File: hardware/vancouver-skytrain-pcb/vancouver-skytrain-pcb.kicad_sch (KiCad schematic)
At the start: 156 parts, among them J2_POWER_IN1 Conn_01x02, J3_PROGRAMING_PIN1 Conn_01x06, Q1 PN2222A, Q2 PN2222A, U1 74AHC1G125, U2 74AHC1G125, U3 74AHC1G125, U4 74AHC1G125

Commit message: positioned all the LEDs, Cap, and 5v Rails
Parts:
- removed C71: 10uF,10V,X5R, vancouver-skytrain-pcb.pretty:C_0603_1608Metric, symbol jlcpcb-basic-capacitor-0603:10uF,10V,X5R
- removed C72, C73: 1uF,25V,X5R, vancouver-skytrain-pcb.pretty:C_0402_1005Metric, symbol jlcpcb-basic-capacitor-0402:1uF,25V,X5R
- removed LED64, LED65: WS2812B, LED_SMD:LED_WS2812B_PLCC4_5.0x5.0mm_P3.2mm, symbol calendar:XL-5050RGBC-WS2812B
- removed U2, U3, U4: 74AHC1G125, Package_TO_SOT_SMD:SOT-23-5, symbol 74xGxx:74AHC1G125
- added C100, C101, C102, C121, C122, C123, C124, C125, C126, C127, C128, C129, C130, C131, C132, C133, C134, C135, C136, C31, C32, C33, C34, C35, C36, C37, C38, C39, C40, C41, C42, C43, C44, C45, C46, C47, C48, C49, C50, C51, C52, C53, C54, C80, C81, C82, C83, C84, C85, C86, C87, C88, C89, C90, C91, C92, C93, C94, C95, C96, C97, C98, C99: 1uF,25V,X5R, vancouver-skytrain-pcb.pretty:C_0402_1005Metric, symbol jlcpcb-basic-capacitor-0402:1uF,25V,X5R
- added C120, C30, C79: 10uF,10V,X5R, vancouver-skytrain-pcb.pretty:C_0603_1608Metric, symbol jlcpcb-basic-capacitor-0603:10uF,10V,X5R
- added LED111, LED112, LED113, LED114, LED115, LED116, LED117, LED118, LED119, LED120, LED121, LED122, LED123, LED124, LED125, LED126, LED25, LED26, LED27, LED28, LED29, LED30, LED31, LED32, LED33, LED34, LED35, LED36, LED37, LED38, LED39, LED40, LED41, LED42, LED43, LED44, LED45, LED46, LED47, LED48, LED72, LED73, LED74, LED75, LED76, LED77, LED78, LED79, LED80, LED81, LED82, LED83, LED84, LED85, LED86, LED87, LED88, LED89, LED90, LED91, LED92, LED93, LED94: WS2812B, vancouver-skytrain-pcb.pretty:XL-1010RGBC-WS2812B, symbol vancouver-skytrain-pcb:XL-1010RGBC-WS2812B
- LED1, LED10, LED11, LED12, LED13, LED14, LED15, LED16, LED17, LED18, LED19, LED2, LED20, LED21, LED22, LED23, LED24, LED3, LED4, LED5, LED6, LED7, LED8, LED9: footprint LED_SMD:LED_WS2812B_PLCC4_5.0x5.0mm_P3.2mm -> vancouver-skytrain-pcb.pretty:XL-1010RGBC-WS2812B; symbol calendar:XL-5050RGBC-WS2812B -> vancouver-skytrain-pcb:XL-1010RGBC-WS2812B; LCSC C2843785 -> C5349953
- LED100: renamed from LED53; footprint LED_SMD:LED_WS2812B_PLCC4_5.0x5.0mm_P3.2mm -> vancouver-skytrain-pcb.pretty:XL-1010RGBC-WS2812B; symbol calendar:XL-5050RGBC-WS2812B -> vancouver-skytrain-pcb:XL-1010RGBC-WS2812B; LCSC C2843785 -> C5349953
- LED101: renamed from LED54; footprint LED_SMD:LED_WS2812B_PLCC4_5.0x5.0mm_P3.2mm -> vancouver-skytrain-pcb.pretty:XL-1010RGBC-WS2812B; symbol calendar:XL-5050RGBC-WS2812B -> vancouver-skytrain-pcb:XL-1010RGBC-WS2812B; LCSC C2843785 -> C5349953
- LED102: renamed from LED55; footprint LED_SMD:LED_WS2812B_PLCC4_5.0x5.0mm_P3.2mm -> vancouver-skytrain-pcb.pretty:XL-1010RGBC-WS2812B; symbol calendar:XL-5050RGBC-WS2812B -> vancouver-skytrain-pcb:XL-1010RGBC-WS2812B; LCSC C2843785 -> C5349953
- LED103: renamed from LED56; footprint LED_SMD:LED_WS2812B_PLCC4_5.0x5.0mm_P3.2mm -> vancouver-skytrain-pcb.pretty:XL-1010RGBC-WS2812B; symbol calendar:XL-5050RGBC-WS2812B -> vancouver-skytrain-pcb:XL-1010RGBC-WS2812B; LCSC C2843785 -> C5349953
- LED104: renamed from LED57; footprint LED_SMD:LED_WS2812B_PLCC4_5.0x5.0mm_P3.2mm -> vancouver-skytrain-pcb.pretty:XL-1010RGBC-WS2812B; symbol calendar:XL-5050RGBC-WS2812B -> vancouver-skytrain-pcb:XL-1010RGBC-WS2812B; LCSC C2843785 -> C5349953
- LED105: renamed from LED58; footprint LED_SMD:LED_WS2812B_PLCC4_5.0x5.0mm_P3.2mm -> vancouver-skytrain-pcb.pretty:XL-1010RGBC-WS2812B; symbol calendar:XL-5050RGBC-WS2812B -> vancouver-skytrain-pcb:XL-1010RGBC-WS2812B; LCSC C2843785 -> C5349953
- LED106: renamed from LED59; footprint LED_SMD:LED_WS2812B_PLCC4_5.0x5.0mm_P3.2mm -> vancouver-skytrain-pcb.pretty:XL-1010RGBC-WS2812B; symbol calendar:XL-5050RGBC-WS2812B -> vancouver-skytrain-pcb:XL-1010RGBC-WS2812B; LCSC C2843785 -> C5349953
- LED107: renamed from LED60; footprint LED_SMD:LED_WS2812B_PLCC4_5.0x5.0mm_P3.2mm -> vancouver-skytrain-pcb.pretty:XL-1010RGBC-WS2812B; symbol calendar:XL-5050RGBC-WS2812B -> vancouver-skytrain-pcb:XL-1010RGBC-WS2812B; LCSC C2843785 -> C5349953
- LED108: renamed from LED61; footprint LED_SMD:LED_WS2812B_PLCC4_5.0x5.0mm_P3.2mm -> vancouver-skytrain-pcb.pretty:XL-1010RGBC-WS2812B; symbol calendar:XL-5050RGBC-WS2812B -> vancouver-skytrain-pcb:XL-1010RGBC-WS2812B; LCSC C2843785 -> C5349953
- LED109: renamed from LED62; footprint LED_SMD:LED_WS2812B_PLCC4_5.0x5.0mm_P3.2mm -> vancouver-skytrain-pcb.pretty:XL-1010RGBC-WS2812B; symbol calendar:XL-5050RGBC-WS2812B -> vancouver-skytrain-pcb:XL-1010RGBC-WS2812B; LCSC C2843785 -> C5349953
- LED110: renamed from LED63; footprint LED_SMD:LED_WS2812B_PLCC4_5.0x5.0mm_P3.2mm -> vancouver-skytrain-pcb.pretty:XL-1010RGBC-WS2812B; symbol calendar:XL-5050RGBC-WS2812B -> vancouver-skytrain-pcb:XL-1010RGBC-WS2812B; LCSC C2843785 -> C5349953
- LED49: renamed from LED25; footprint LED_SMD:LED_WS2812B_PLCC4_5.0x5.0mm_P3.2mm -> vancouver-skytrain-pcb.pretty:XL-1010RGBC-WS2812B; symbol calendar:XL-5050RGBC-WS2812B -> vancouver-skytrain-pcb:XL-1010RGBC-WS2812B; LCSC C2843785 -> C5349953
- LED50: renamed from LED26; footprint LED_SMD:LED_WS2812B_PLCC4_5.0x5.0mm_P3.2mm -> vancouver-skytrain-pcb.pretty:XL-1010RGBC-WS2812B; symbol calendar:XL-5050RGBC-WS2812B -> vancouver-skytrain-pcb:XL-1010RGBC-WS2812B; LCSC C2843785 -> C5349953
- LED51: renamed from LED27; footprint LED_SMD:LED_WS2812B_PLCC4_5.0x5.0mm_P3.2mm -> vancouver-skytrain-pcb.pretty:XL-1010RGBC-WS2812B; symbol calendar:XL-5050RGBC-WS2812B -> vancouver-skytrain-pcb:XL-1010RGBC-WS2812B; LCSC C2843785 -> C5349953
- LED52: renamed from LED28; footprint LED_SMD:LED_WS2812B_PLCC4_5.0x5.0mm_P3.2mm -> vancouver-skytrain-pcb.pretty:XL-1010RGBC-WS2812B; symbol calendar:XL-5050RGBC-WS2812B -> vancouver-skytrain-pcb:XL-1010RGBC-WS2812B; LCSC C2843785 -> C5349953
- LED53: renamed from LED29; footprint LED_SMD:LED_WS2812B_PLCC4_5.0x5.0mm_P3.2mm -> vancouver-skytrain-pcb.pretty:XL-1010RGBC-WS2812B; symbol calendar:XL-5050RGBC-WS2812B -> vancouver-skytrain-pcb:XL-1010RGBC-WS2812B; LCSC C2843785 -> C5349953
- LED54: renamed from LED30; footprint LED_SMD:LED_WS2812B_PLCC4_5.0x5.0mm_P3.2mm -> vancouver-skytrain-pcb.pretty:XL-1010RGBC-WS2812B; symbol calendar:XL-5050RGBC-WS2812B -> vancouver-skytrain-pcb:XL-1010RGBC-WS2812B; LCSC C2843785 -> C5349953
- LED55: renamed from LED31; footprint LED_SMD:LED_WS2812B_PLCC4_5.0x5.0mm_P3.2mm -> vancouver-skytrain-pcb.pretty:XL-1010RGBC-WS2812B; symbol calendar:XL-5050RGBC-WS2812B -> vancouver-skytrain-pcb:XL-1010RGBC-WS2812B; LCSC C2843785 -> C5349953
- LED56: renamed from LED32; footprint LED_SMD:LED_WS2812B_PLCC4_5.0x5.0mm_P3.2mm -> vancouver-skytrain-pcb.pretty:XL-1010RGBC-WS2812B; symbol calendar:XL-5050RGBC-WS2812B -> vancouver-skytrain-pcb:XL-1010RGBC-WS2812B; LCSC C2843785 -> C5349953
- LED57: renamed from LED33; footprint LED_SMD:LED_WS2812B_PLCC4_5.0x5.0mm_P3.2mm -> vancouver-skytrain-pcb.pretty:XL-1010RGBC-WS2812B; symbol calendar:XL-5050RGBC-WS2812B -> vancouver-skytrain-pcb:XL-1010RGBC-WS2812B; LCSC C2843785 -> C5349953
- LED58: renamed from LED34; footprint LED_SMD:LED_WS2812B_PLCC4_5.0x5.0mm_P3.2mm -> vancouver-skytrain-pcb.pretty:XL-1010RGBC-WS2812B; symbol calendar:XL-5050RGBC-WS2812B -> vancouver-skytrain-pcb:XL-1010RGBC-WS2812B; LCSC C2843785 -> C5349953
- LED59: renamed from LED35; footprint LED_SMD:LED_WS2812B_PLCC4_5.0x5.0mm_P3.2mm -> vancouver-skytrain-pcb.pretty:XL-1010RGBC-WS2812B; symbol calendar:XL-5050RGBC-WS2812B -> vancouver-skytrain-pcb:XL-1010RGBC-WS2812B; LCSC C2843785 -> C5349953
- LED60: renamed from LED36; footprint LED_SMD:LED_WS2812B_PLCC4_5.0x5.0mm_P3.2mm -> vancouver-skytrain-pcb.pretty:XL-1010RGBC-WS2812B; symbol calendar:XL-5050RGBC-WS2812B -> vancouver-skytrain-pcb:XL-1010RGBC-WS2812B; LCSC C2843785 -> C5349953
- LED61: renamed from LED37; footprint LED_SMD:LED_WS2812B_PLCC4_5.0x5.0mm_P3.2mm -> vancouver-skytrain-pcb.pretty:XL-1010RGBC-WS2812B; symbol calendar:XL-5050RGBC-WS2812B -> vancouver-skytrain-pcb:XL-1010RGBC-WS2812B; LCSC C2843785 -> C5349953
- LED62: renamed from LED38; footprint LED_SMD:LED_WS2812B_PLCC4_5.0x5.0mm_P3.2mm -> vancouver-skytrain-pcb.pretty:XL-1010RGBC-WS2812B; symbol calendar:XL-5050RGBC-WS2812B -> vancouver-skytrain-pcb:XL-1010RGBC-WS2812B; LCSC C2843785 -> C5349953
- LED63: renamed from LED39; footprint LED_SMD:LED_WS2812B_PLCC4_5.0x5.0mm_P3.2mm -> vancouver-skytrain-pcb.pretty:XL-1010RGBC-WS2812B; symbol calendar:XL-5050RGBC-WS2812B -> vancouver-skytrain-pcb:XL-1010RGBC-WS2812B; LCSC C2843785 -> C5349953
- LED64: renamed from LED40; footprint LED_SMD:LED_WS2812B_PLCC4_5.0x5.0mm_P3.2mm -> vancouver-skytrain-pcb.pretty:XL-1010RGBC-WS2812B; symbol calendar:XL-5050RGBC-WS2812B -> vancouver-skytrain-pcb:XL-1010RGBC-WS2812B; LCSC C2843785 -> C5349953
- LED65: renamed from LED41; footprint LED_SMD:LED_WS2812B_PLCC4_5.0x5.0mm_P3.2mm -> vancouver-skytrain-pcb.pretty:XL-1010RGBC-WS2812B; symbol calendar:XL-5050RGBC-WS2812B -> vancouver-skytrain-pcb:XL-1010RGBC-WS2812B; LCSC C2843785 -> C5349953
- LED66: renamed from LED42; footprint LED_SMD:LED_WS2812B_PLCC4_5.0x5.0mm_P3.2mm -> vancouver-skytrain-pcb.pretty:XL-1010RGBC-WS2812B; symbol calendar:XL-5050RGBC-WS2812B -> vancouver-skytrain-pcb:XL-1010RGBC-WS2812B; LCSC C2843785 -> C5349953
- LED67: renamed from LED43; footprint LED_SMD:LED_WS2812B_PLCC4_5.0x5.0mm_P3.2mm -> vancouver-skytrain-pcb.pretty:XL-1010RGBC-WS2812B; symbol calendar:XL-5050RGBC-WS2812B -> vancouver-skytrain-pcb:XL-1010RGBC-WS2812B; LCSC C2843785 -> C5349953
- LED68: renamed from LED44; footprint LED_SMD:LED_WS2812B_PLCC4_5.0x5.0mm_P3.2mm -> vancouver-skytrain-pcb.pretty:XL-1010RGBC-WS2812B; symbol calendar:XL-5050RGBC-WS2812B -> vancouver-skytrain-pcb:XL-1010RGBC-WS2812B; LCSC C2843785 -> C5349953
- LED69: renamed from LED45; footprint LED_SMD:LED_WS2812B_PLCC4_5.0x5.0mm_P3.2mm -> vancouver-skytrain-pcb.pretty:XL-1010RGBC-WS2812B; symbol calendar:XL-5050RGBC-WS2812B -> vancouver-skytrain-pcb:XL-1010RGBC-WS2812B; LCSC C2843785 -> C5349953
- LED70: renamed from LED46; footprint LED_SMD:LED_WS2812B_PLCC4_5.0x5.0mm_P3.2mm -> vancouver-skytrain-pcb.pretty:XL-1010RGBC-WS2812B; symbol calendar:XL-5050RGBC-WS2812B -> vancouver-skytrain-pcb:XL-1010RGBC-WS2812B; LCSC C2843785 -> C5349953
- LED71: renamed from LED47; footprint LED_SMD:LED_WS2812B_PLCC4_5.0x5.0mm_P3.2mm -> vancouver-skytrain-pcb.pretty:XL-1010RGBC-WS2812B; symbol calendar:XL-5050RGBC-WS2812B -> vancouver-skytrain-pcb:XL-1010RGBC-WS2812B; LCSC C2843785 -> C5349953
- LED95: renamed from LED48; footprint LED_SMD:LED_WS2812B_PLCC4_5.0x5.0mm_P3.2mm -> vancouver-skytrain-pcb.pretty:XL-1010RGBC-WS2812B; symbol calendar:XL-5050RGBC-WS2812B -> vancouver-skytrain-pcb:XL-1010RGBC-WS2812B; LCSC C2843785 -> C5349953
- LED96: renamed from LED49; footprint LED_SMD:LED_WS2812B_PLCC4_5.0x5.0mm_P3.2mm -> vancouver-skytrain-pcb.pretty:XL-1010RGBC-WS2812B; symbol calendar:XL-5050RGBC-WS2812B -> vancouver-skytrain-pcb:XL-1010RGBC-WS2812B; LCSC C2843785 -> C5349953
- LED97: renamed from LED50; footprint LED_SMD:LED_WS2812B_PLCC4_5.0x5.0mm_P3.2mm -> vancouver-skytrain-pcb.pretty:XL-1010RGBC-WS2812B; symbol calendar:XL-5050RGBC-WS2812B -> vancouver-skytrain-pcb:XL-1010RGBC-WS2812B; LCSC C2843785 -> C5349953
- LED98: renamed from LED51; footprint LED_SMD:LED_WS2812B_PLCC4_5.0x5.0mm_P3.2mm -> vancouver-skytrain-pcb.pretty:XL-1010RGBC-WS2812B; symbol calendar:XL-5050RGBC-WS2812B -> vancouver-skytrain-pcb:XL-1010RGBC-WS2812B; LCSC C2843785 -> C5349953
- LED99: renamed from LED52; footprint LED_SMD:LED_WS2812B_PLCC4_5.0x5.0mm_P3.2mm -> vancouver-skytrain-pcb.pretty:XL-1010RGBC-WS2812B; symbol calendar:XL-5050RGBC-WS2812B -> vancouver-skytrain-pcb:XL-1010RGBC-WS2812B; LCSC C2843785 -> C5349953
- renumbered C54 to C103, C55 to C104, C56 to C105, C57 to C106, C58 to C107, C59 to C108, C60 to C109, C61 to C110, C62 to C111, C63 to C112, C64 to C113, C65 to C114, C66 to C115, C67 to C116, C68 to C117, C69 to C118, C70 to C119, C30 to C55, C31 to C56, C32 to C57, C33 to C58, C34 to C59, C35 to C60, C36 to C61, C37 to C62, C38 to C63, C39 to C64, C40 to C65, C41 to C66, C42 to C67, C43 to C68, C44 to C69, C45 to C70, C46 to C71, C47 to C72, C48 to C73, C49 to C74, C50 to C75, C51 to C76, C52 to C77, C53 to C78
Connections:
- net +5V: now also LED1.2 (VDD), LED10.2 (VDD), LED100.2 (VDD), LED101.2 (VDD), LED102.2 (VDD), LED103.2 (VDD), LED104.2 (VDD), LED105.2 (VDD), LED106.2 (VDD), LED107.2 (VDD), LED108.2 (VDD), LED109.2 (VDD), LED11.2 (VDD), LED110.2 (VDD), LED12.2 (VDD), LED13.2 (VDD), LED14.2 (VDD), LED15.2 (VDD), LED16.2 (VDD), LED17.2 (VDD), LED18.2 (VDD), LED19.2 (VDD), LED2.2 (VDD), LED20.2 (VDD), LED21.2 (VDD), LED22.2 (VDD), LED23.2 (VDD), LED24.2 (VDD), LED3.2 (VDD), LED4.2 (VDD), LED49.2 (VDD), LED5.2 (VDD), LED50.2 (VDD), LED51.2 (VDD), LED52.2 (VDD), LED53.2 (VDD), LED54.2 (VDD), LED55.2 (VDD), LED56.2 (VDD), LED57.2 (VDD)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; no longer LED1.1 (VDD), LED10.1 (VDD), LED100.1 (VDD), LED101.1 (VDD), LED102.1 (VDD), LED103.1 (VDD), LED104.1 (VDD), LED105.1 (VDD), LED106.1 (VDD), LED107.1 (VDD), LED108.1 (VDD), LED109.1 (VDD), LED11.1 (VDD), LED110.1 (VDD), LED12.1 (VDD), LED13.1 (VDD), LED14.1 (VDD), LED15.1 (VDD), LED16.1 (VDD), LED17.1 (VDD), LED18.1 (VDD), LED19.1 (VDD), LED2.1 (VDD), LED20.1 (VDD), LED21.1 (VDD), LED22.1 (VDD), LED23.1 (VDD), LED24.1 (VDD), LED3.1 (VDD), LED4.1 (VDD), LED49.1 (VDD), LED5.1 (VDD), LED50.1 (VDD), LED51.1 (VDD), LED52.1 (VDD), LED53.1 (VDD), LED54.1 (VDD), LED55.1 (VDD), LED56.1 (VDD), LED57.1 (VDD)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
- net GND: now also C100.2, C101.2, C102.2, C120.1, C121.2, C122.2, C123.2, C124.2, C125.2, C126.2, C127.2, C128.2, C129.2, C130.2, C131.2, C132.2, C133.2, C134.2, C135.2, C136.2, C30.1, C31.2, C32.2, C33.2, C34.2, C35.2, C36.2, C37.2, C38.2, C39.2, C40.2, C41.2, C42.2, C43.2, C44.2, C45.2, C46.2, C47.2, C48.2, C49.2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
- net SW_BRIGHTNESS: no longer U_CPU1.30 (IO18)
- net at LED70.4 (DIN): now also LED69.1 (DOUT); no longer LED69.2 (DOU)
- net at LED69.4 (DIN): now also LED68.1 (DOUT); no longer LED68.2 (DOU)
- net at LED24.4 (DIN): now also LED23.1 (DOUT); no longer LED23.2 (DOU)
- net at LED23.4 (DIN): now also LED22.1 (DOUT); no longer LED22.2 (DOU)
- net at LED20.4 (DIN): now also LED19.1 (DOUT); no longer LED19.2 (DOU)
- net at LED19.4 (DIN): now also LED18.1 (DOUT); no longer LED18.2 (DOU)
- net LEDS_EXPO_LINE_EAST_TO_WEST: now reaches LED1.4 (DIN), U1.4
- net LEDS_CANADA_LINE_SOUTH_TO_NORTH: now reaches LED95.4 (DIN)
- net LEDS_CANADA_LINE_SOUTH_TO_NORTH: now also LED94.1 (DOUT)
- net at LED18.4 (DIN): now also LED17.1 (DOUT); no longer LED17.2 (DOU)
- net at LED110.4 (DIN): now also LED109.1 (DOUT); no longer LED109.2 (DOU)
- net at LED109.4 (DIN): now also LED108.1 (DOUT); no longer LED108.2 (DOU)
- net at LED54.4 (DIN): now also LED53.1 (DOUT); no longer LED53.2 (DOU)
- net at LED53.4 (DIN): now also LED52.1 (DOUT); no longer LED52.2 (DOU)
- net at LED17.4 (DIN): now also LED16.1 (DOUT); no longer LED16.2 (DOU)
- net at LED106.4 (DIN): now also LED105.1 (DOUT); no longer LED105.2 (DOU)
- net at LED105.4 (DIN): now also LED104.1 (DOUT); no longer LED104.2 (DOU)
- net at LED16.4 (DIN): now also LED15.1 (DOUT); no longer LED15.2 (DOU)
- net at LED15.4 (DIN): now also LED14.1 (DOUT); no longer LED14.2 (DOU)
- net at LED11.4 (DIN): now also LED10.1 (DOUT); no longer LED10.2 (DOU)
- net at LED10.4 (DIN): now also LED9.1 (DOUT); no longer LED9.2 (DOU)
- net at LED71.4 (DIN): now also LED70.1 (DOUT); no longer LED70.2 (DOU)
- net at LED9.4 (DIN): now also LED8.1 (DOUT); no longer LED8.2 (DOU)
- net at LED8.4 (DIN): now also LED7.1 (DOUT); no longer LED7.2 (DOU)
- net at LED63.4 (DIN): now also LED62.1 (DOUT); no longer LED62.2 (DOU)
- net at LED62.4 (DIN): now also LED61.1 (DOUT); no longer LED61.2 (DOU)
- net at LED108.4 (DIN): now also LED107.1 (DOUT); no longer LED107.2 (DOU)
- net at LED50.4 (DIN): now also LED49.1 (DOUT); no longer LED49.2 (DOU)
- net LEDS_MILLENNIUM_LINE_EAST_TO_WEST: now reaches LED49.4 (DIN)
- net LEDS_MILLENNIUM_LINE_EAST_TO_WEST: now also LED48.1 (DOUT)
- net at LED65.4 (DIN): now also LED64.1 (DOUT); no longer LED64.2 (DOU)
- net at LED64.4 (DIN): now also LED63.1 (DOUT); no longer LED63.2 (DOU)
- net at LED98.4 (DIN): now also LED97.1 (DOUT); no longer LED97.2 (DOU)
- net at LED97.4 (DIN): now also LED96.1 (DOUT); no longer LED96.2 (DOU)
- net at LED52.4 (DIN): now also LED51.1 (DOUT); no longer LED51.2 (DOU)
- net at LED14.4 (DIN): now also LED13.1 (DOUT); no longer LED13.2 (DOU)
- net at LED61.4 (DIN): now also LED60.1 (DOUT); no longer LED60.2 (DOU)
- net at LED96.4 (DIN): now also LED95.1 (DOUT); no longer LED95.2 (DOU)
- net at LED107.4 (DIN): now also LED106.1 (DOUT); no longer LED106.2 (DOU)
- net at LED51.4 (DIN): now also LED50.1 (DOUT); no longer LED50.2 (DOU)
- net at LED55.4 (DIN): now also LED54.1 (DOUT); no longer LED54.2 (DOU)
- net at LED5.4 (DIN): now also LED4.1 (DOUT); no longer LED4.2 (DOU)
- net at LED4.4 (DIN): now also LED3.1 (DOUT); no longer LED3.2 (DOU)
- net at LED104.4 (DIN): now also LED103.1 (DOUT); no longer LED103.2 (DOU)
- net at LED103.4 (DIN): now also LED102.1 (DOUT); no longer LED102.2 (DOU)
- net at LED13.4 (DIN): now also LED12.1 (DOUT); no longer LED12.2 (DOU)
- net at LED12.4 (DIN): now also LED11.1 (DOUT); no longer LED11.2 (DOU)
- net at LED57.4 (DIN): now also LED56.1 (DOUT); no longer LED56.2 (DOU)
- net at LED56.4 (DIN): now also LED55.1 (DOUT); no longer LED55.2 (DOU)
- net at LED67.4 (DIN): now also LED66.1 (DOUT); no longer LED66.2 (DOU)
- net at LED66.4 (DIN): now also LED65.1 (DOUT); no longer LED65.2 (DOU)
- net at LED99.4 (DIN): now also LED98.1 (DOUT); no longer LED98.2 (DOU)
- net at LED100.4 (DIN): now also LED99.1 (DOUT); no longer LED99.2 (DOU)
- net at LED7.4 (DIN): now also LED6.1 (DOUT); no longer LED6.2 (DOU)
- net at LED6.4 (DIN): now also LED5.1 (DOUT); no longer LED5.2 (DOU)
- net at LED22.4 (DIN): now also LED21.1 (DOUT); no longer LED21.2 (DOU)
- net at LED21.4 (DIN): now also LED20.1 (DOUT); no longer LED20.2 (DOU)
- net at LED68.4 (DIN): now also LED67.1 (DOUT); no longer LED67.2 (DOU)
- net at LED102.4 (DIN): now also LED101.1 (DOUT); no longer LED101.2 (DOU)
- net at LED2.4 (DIN): now also LED1.1 (DOUT); no longer LED1.2 (DOU)
- net at LED58.4 (DIN): now also LED57.1 (DOUT); no longer LED57.2 (DOU)
- net at LED59.4 (DIN): now also LED58.1 (DOUT); no longer LED58.2 (DOU)
- net at LED101.4 (DIN): now also LED100.1 (DOUT); no longer LED100.2 (DOU)
- net at LED60.4 (DIN): now also LED59.1 (DOUT); no longer LED59.2 (DOU)
- net at LED3.4 (DIN): now also LED2.1 (DOUT); no longer LED2.2 (DOU)
- net LEDS_CANADA_LINE: no longer names the net of U_CPU1.27 (IO16)
- net LEDS_EXPO_LINE renamed LED_IN
- net LEDS_MILLENNIUM_LINE: no longer names the net of U_CPU1.23 (IO15)
- net LEDS_SEA_BUS_LINE: no longer names the net of U_CPU1.28 (IO17)
- new net: LED80.1 (DOUT), LED81.4 (DIN)
- new net: LED79.1 (DOUT), LED80.4 (DIN)
- new net: LED27.1 (DOUT), LED28.4 (DIN)
- new net: LED26.1 (DOUT), LED27.4 (DIN)
- new net: LED77.1 (DOUT), LED78.4 (DIN)
- new net: LED76.1 (DOUT), LED77.4 (DIN)
- new net: LED90.1 (DOUT), LED91.4 (DIN)
- new net: LED89.1 (DOUT), LED90.4 (DIN)
- new net: LED42.1 (DOUT), LED43.4 (DIN)
- new net: LED41.1 (DOUT), LED42.4 (DIN)
- new net: LED73.1 (DOUT), LED74.4 (DIN)
- new net: LED72.1 (DOUT), LED73.4 (DIN)
- new net: LED124.1 (DOUT), LED125.4 (DIN)
- new net: LED123.1 (DOUT), LED124.4 (DIN)
- new net: LED29.1 (DOUT), LED30.4 (DIN)
- new net: LED28.1 (DOUT), LED29.4 (DIN)
- new net: LED112.1 (DOUT), LED113.4 (DIN)
- new net: LED111.1 (DOUT), LED112.4 (DIN)
- new net: LED34.1 (DOUT), LED35.4 (DIN)
- new net: LED33.1 (DOUT), LED34.4 (DIN)
- new net: LED40.1 (DOUT), LED41.4 (DIN)
- new net: LED39.1 (DOUT), LED40.4 (DIN)
- new net: LED25.1 (DOUT), LED26.4 (DIN)
- new net: LED120.1 (DOUT), LED121.4 (DIN)
- new net: LED119.1 (DOUT), LED120.4 (DIN)
- new net: LED37.1 (DOUT), LED38.4 (DIN)
- new net: LED36.1 (DOUT), LED37.4 (DIN)
- new net: LED35.1 (DOUT), LED36.4 (DIN)
- new net: LED83.1 (DOUT), LED84.4 (DIN)
- new net: LED82.1 (DOUT), LED83.4 (DIN)
- new net: LED91.1 (DOUT), LED92.4 (DIN)
- new net: LED38.1 (DOUT), LED39.4 (DIN)
- new net: LED87.1 (DOUT), LED88.4 (DIN)
- new net: LED86.1 (DOUT), LED87.4 (DIN)
- new net: LED45.1 (DOUT), LED46.4 (DIN)
- new net: LED44.1 (DOUT), LED45.4 (DIN)
- new net: LED125.1 (DOUT), LED126.4 (DIN)
- new net: LED47.1 (DOUT), LED48.4 (DIN)
- new net: LED114.1 (DOUT), LED115.4 (DIN)
- new net: LED113.1 (DOUT), LED114.4 (DIN)
- new net: LED93.1 (DOUT), LED94.4 (DIN)
- new net: LED92.1 (DOUT), LED93.4 (DIN)
- new net: LED74.1 (DOUT), LED75.4 (DIN)
- new net: LED117.1 (DOUT), LED118.4 (DIN)
- new net: LED116.1 (DOUT), LED117.4 (DIN)
- new net: LED46.1 (DOUT), LED47.4 (DIN)
- new net: LED75.1 (DOUT), LED76.4 (DIN)
- new net: LED121.1 (DOUT), LED122.4 (DIN)
- new net: LED81.1 (DOUT), LED82.4 (DIN)
- new net: LED43.1 (DOUT), LED44.4 (DIN)
- new net: LED118.1 (DOUT), LED119.4 (DIN)
- new net: LED85.1 (DOUT), LED86.4 (DIN)
- new net: LED115.1 (DOUT), LED116.4 (DIN)
- new net: LED32.1 (DOUT), LED33.4 (DIN)
- new net: LED88.1 (DOUT), LED89.4 (DIN)
- new net: LED31.1 (DOUT), LED32.4 (DIN)
- new net: LED30.1 (DOUT), LED31.4 (DIN)
- new net: LED84.1 (DOUT), LED85.4 (DIN)
- new net: LED122.1 (DOUT), LED123.4 (DIN)
- new net: LED78.1 (DOUT), LED79.4 (DIN)
- new net LEDS_CANADA_LINE_NORTH_TO_SOUTH: LED110.1 (DOUT), LED111.4 (DIN)
- new net LEDS_EXPO_LINE_WEST_TO_EAST: LED24.1 (DOUT), LED25.4 (DIN)
- new net LEDS_MILLENNIUM_LINE_WEST_TO_EAST: LED71.1 (DOUT), LED72.4 (DIN)
- new net LED_OUT: LED126.1 (DOUT)
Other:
- moved on the sheet: C103, C104, C105, C106, C107, C108, C109, C110, C111, C112, C113, C114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

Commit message: Resolved a bunch of DRC errors
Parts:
- removed C103, C120, C30, C5, C55, C79: 10uF,10V,X5R, vancouver-skytrain-pcb.pretty:C_0603_1608Metric, symbol jlcpcb-basic-capacitor-0603:10uF,10V,X5R
- removed SW_BRIGHTNESS1: Switch_SW_Push, Button_Switch_SMD:SW_Push_1P1T_NO_6x6mm_H9.5mm, symbol tom-mechanical:SW_SPST
- added C131: 1uF,25V,X5R, vancouver-skytrain-pcb.pretty:C_0402_1005Metric, symbol jlcpcb-basic-capacitor-0402:1uF,25V,X5R
- added H1, H2, H3, H4: MountingHole, MountingHole:MountingHole_3.2mm_M3, symbol Mechanical:MountingHole
- added J1: Conn_01x04, Connector_PinHeader_2.54mm:PinHeader_1x04_P2.54mm_Vertical, symbol Connector_Generic:Conn_01x04
- added LED127: WS2812B, vancouver-skytrain-pcb.pretty:XL-1010RGBC-WS2812B, symbol vancouver-skytrain-pcb:XL-1010RGBC-WS2812B
- added R2: 0, Resistor_SMD:R_0402_1005Metric, symbol jlcpcb-basic-resistor-0402:0
- renumbered C11 to C10, C105 to C100, C106 to C101, C107 to C102, C108 to C103, C109 to C104, C110 to C105, C111 to C106, C112 to C107, C113 to C108, C114 to C109, C12 to C11, C115 to C110, C116 to C111, C117 to C112, C118 to C113, C119 to C114, C121 to C115, C122 to C116, C123 to C117, C124 to C118, C125 to C119, C13 to C12, C126 to C120, C127 to C121, C128 to C122, C129 to C123, C130 to C124, C131 to C125, C132 to C126, C133 to C127, C134 to C128, C135 to C129, C14 to C13, C136 to C130, C15 to C14, C16 to C15, C17 to C16, C18 to C17, C19 to C18, C20 to C19, C21 to C20, C22 to C21, C23 to C22, C24 to C23, C25 to C24, C26 to C25, C27 to C26, C28 to C27, C29 to C28, C31 to C29, C32 to C30, C33 to C31, C34 to C32, C35 to C33, C36 to C34, C37 to C35, C38 to C36, C39 to C37, C40 to C38, C41 to C39, C42 to C40, C43 to C41, C44 to C42, C45 to C43, C46 to C44, C47 to C45, C48 to C46, C49 to C47, C50 to C48, C51 to C49, C6 to C5, C52 to C50, C53 to C51, C54 to C52, C56 to C53, C57 to C54, C58 to C55, C59 to C56, C60 to C57, C61 to C58, C62 to C59, C7 to C6, C63 to C60, C64 to C61, C65 to C62, C66 to C63, C67 to C64, C68 to C65, C69 to C66, C70 to C67, C71 to C68, C72 to C69, C8 to C7, C73 to C70, C74 to C71, C75 to C72, C76 to C73, C77 to C74, C78 to C75, C80 to C76, C81 to C77, C82 to C78, C83 to C79, C9 to C8, C84 to C80, C85 to C81, C86 to C82, C87 to C83, C88 to C84, C89 to C85, C90 to C86, C91 to C87, C92 to C88, C93 to C89, C10 to C9, C94 to C90, C95 to C91, C96 to C92, C97 to C93, C98 to C94, C99 to C95, C100 to C96, C101 to C97, C102 to C98, C104 to C99, R2 to R3, R3 to R4, R4 to R5
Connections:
- net +5V: now also C131.1, J1.1 (Pin_1), LED127.2 (VDD)
- net GND: now also C131.2, J1.3 (Pin_3), LED127.3 (VSS)
- net LED_IN: now also J1.2 (Pin_2), R2.2; no longer U_CPU1.13 (IO14)
- net LED_OUT: now also J1.4 (Pin_4), LED127.1 (DOUT); no longer LED126.1 (DOUT)
- new net: R2.1, U_CPU1.13 (IO14)
- new net LEDS_SEA_BUS: LED126.1 (DOUT), LED127.4 (DIN)
- no-connect marks 3 -> 22

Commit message: Clean up before sending to fab
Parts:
- U_POWER1: value LT1117-3.3 -> UR133AG-33-AB3-C-R__3.3v; footprint Package_TO_SOT_SMD:TO-263-3_TabPin2 -> Package_TO_SOT_SMD:SOT-89-3; LCSC C498315 -> C73288
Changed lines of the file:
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@@
   )
   (symbol (lib_id "Regulator_Linear:LT1117-3.3") (at 130.175 36.195 0) (unit 1)
-    (in_bom yes) (on_board yes) (dnp no) (fields_autoplaced)
+    (in_bom yes) (on_board yes) (dnp no)
     (property "Reference" "U_POWER1" (at 130.175 28.575 0)
       (effects (font (size 1.27 1.27)))
     )
-    (property "Value" "LT1117-3.3" (at 130.175 31.115 0)
+    (property "Value" "UR133AG-33-AB3-C-R__3.3v" (at 130.81 25.4 0)
       (effects (font (size 1.27 1.27)))
     )
-    (property "Footprint" "Package_TO_SOT_SMD:TO-263-3_TabPin2" (at 130.175 36.195 0)
+    (property "Footprint" "Package_TO_SOT_SMD:SOT-89-3" (at 130.175 36.195 0)
       (effects (font (size 1.27 1.27)) hide)
     )
-    (property "Datasheet" "https://www.analog.com/media/en/technical-documentation/data-sheets/1117fd.pdf" (at 130.175 36.195 0)
+    (property "Datasheet" "https://datasheet.lcsc.com/lcsc/2304140030_UTC-Unisonic-Tech-UR133AG-33-AB3-C-R_C73288.pdf" (at 130.175 36.195 0)
       (effects (font (size 1.27 1.27)) hide)
     )
-    (property "LCSC" "C498315" (at 130.175 36.195 0)
+    (property "LCSC" "C73288" (at 130.175 36.195 0)
       (effects (font (size 1.27 1.27)) hide)
     )

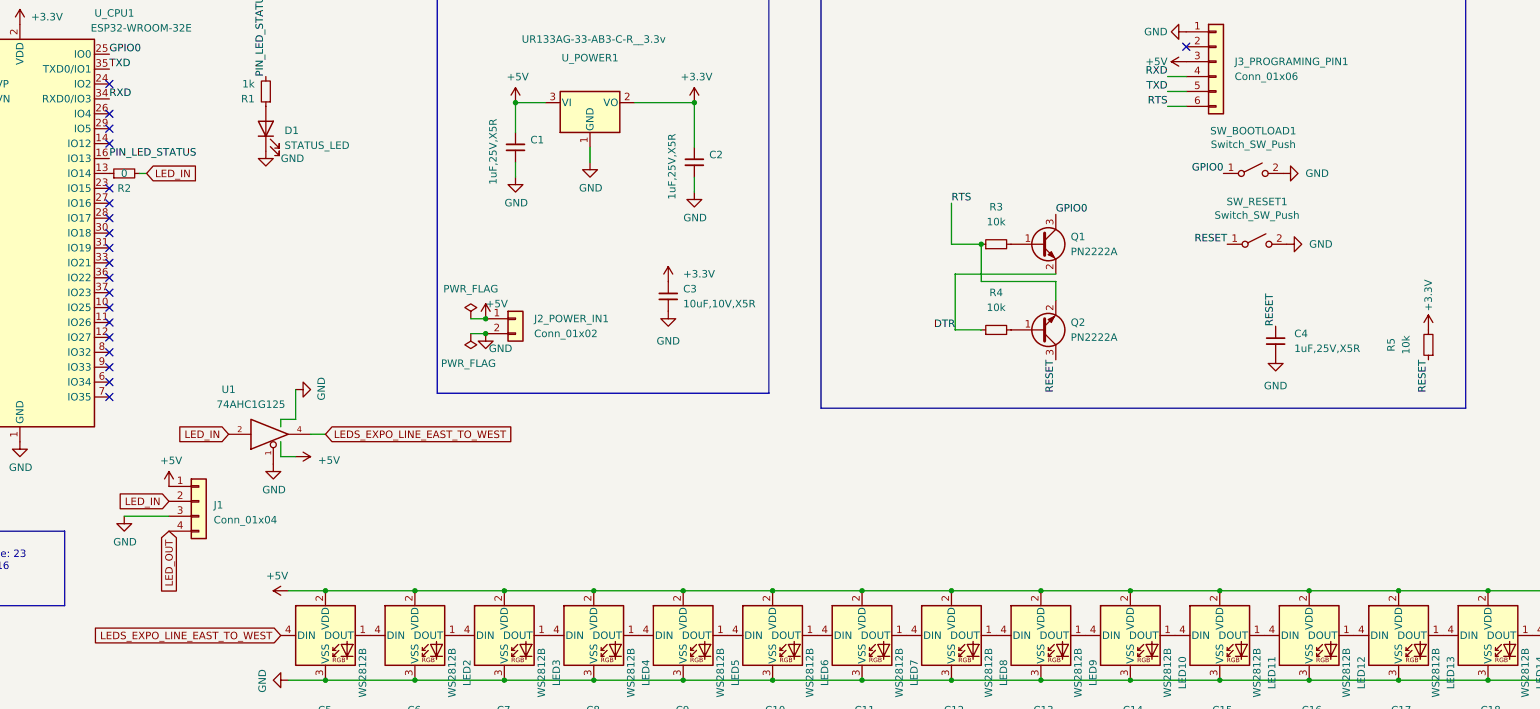
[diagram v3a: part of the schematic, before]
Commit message: Updated headers and update to kicad v8
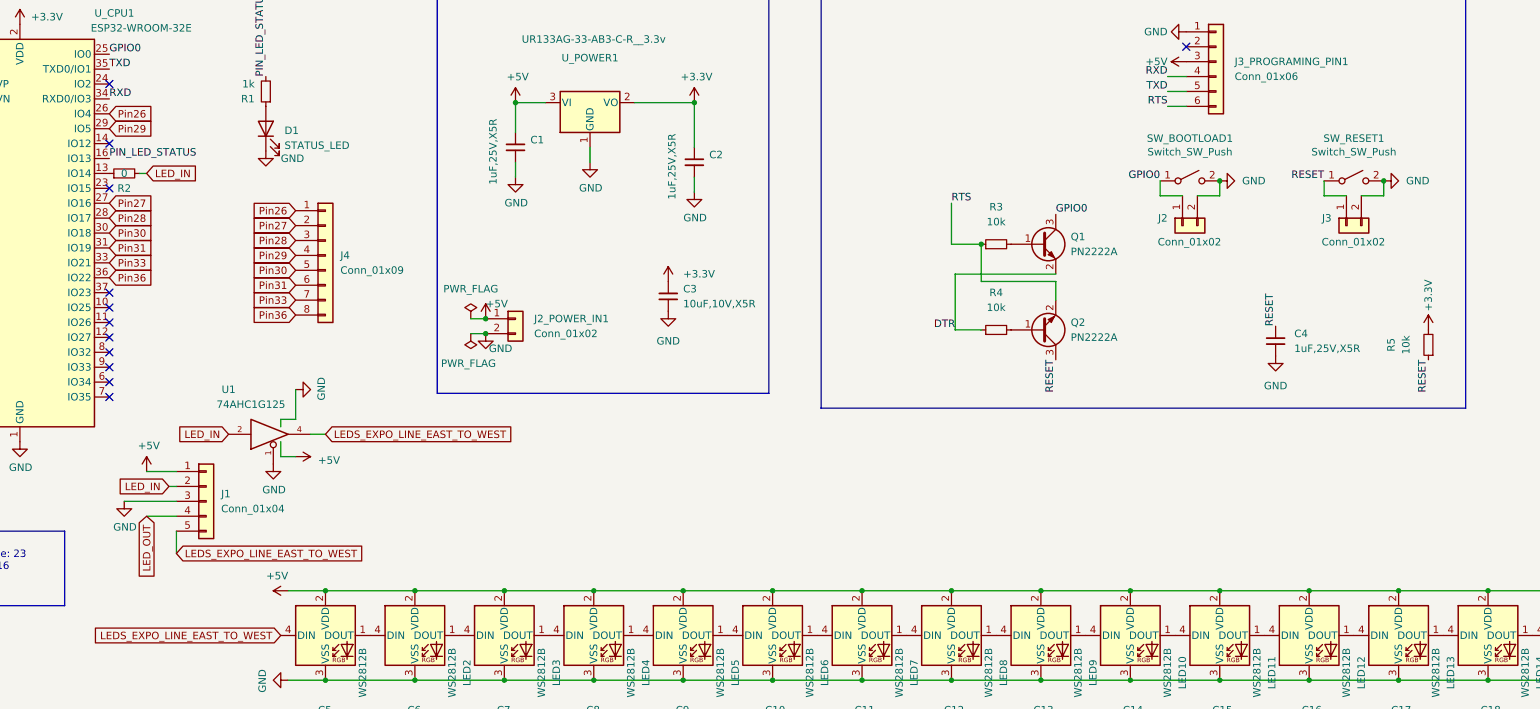
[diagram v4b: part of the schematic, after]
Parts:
- added J2, J3: Conn_01x02, Connector_PinHeader_2.54mm:PinHeader_1x02_P2.54mm_Vertical, symbol Connector_Generic:Conn_01x02
- added J4: Conn_01x09, Connector_PinHeader_2.54mm:PinHeader_1x08_P2.54mm_Vertical, symbol Connector_Generic:Conn_01x08
- J1: footprint Connector_PinHeader_2.54mm:PinHeader_1x04_P2.54mm_Vertical -> Connector_PinHeader_2.54mm:PinHeader_1x05_P2.54mm_Vertical; symbol Connector_Generic:Conn_01x04 -> Connector_Generic:Conn_01x05
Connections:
- net GND: now also J2.2 (Pin_2), J3.2 (Pin_2)
- net GPIO0: now also J2.1 (Pin_1)
- net LEDS_EXPO_LINE_EAST_TO_WEST: now also J1.5 (Pin_5)
- net RESET: now also J3.1 (Pin_1)
- net Pin26: now reaches U_CPU1.26 (IO4)
- net Pin26: now also J4.1 (Pin_1)
- net Pin27: now reaches U_CPU1.27 (IO16)
- net Pin27: now also J4.2 (Pin_2)
- net Pin28: now reaches U_CPU1.28 (IO17)
- net Pin28: now also J4.3 (Pin_3)
- net Pin29: now reaches U_CPU1.29 (IO5)
- net Pin29: now also J4.4 (Pin_4)
- net Pin30: now reaches U_CPU1.30 (IO18)
- net Pin30: now also J4.5 (Pin_5)
- net Pin31: now reaches U_CPU1.31 (IO19)
- net Pin31: now also J4.6 (Pin_6)
- net Pin33: now reaches U_CPU1.33 (IO21)
- net Pin33: now also J4.7 (Pin_7)
- net Pin36: now reaches U_CPU1.36 (IO22)
- net Pin36: now also J4.8 (Pin_8)
- no-connect marks 22 -> 14
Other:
- moved on the sheet: SW_BOOTLOAD1, SW_RESET1

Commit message: Added test points for all leds that look like bugs
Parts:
- added TP1, TP10, TP100, TP101, TP102, TP103, TP104, TP105, TP106, TP107, TP108, TP109, TP11, TP110, TP111, TP112, TP113, TP114, TP115, TP116, TP117, TP118, TP119, TP12, TP120, TP121, TP122, TP123, TP124, TP125, TP126, TP13, TP14, TP15, TP16, TP17, TP18, TP19, TP2, TP20, TP21, TP22, TP23, TP24, TP25, TP26, TP27, TP28, TP29, TP3, TP30, TP31, TP32, TP33, TP34, TP35, TP36, TP37, TP38, TP39, TP4, TP40, TP41, TP42, TP43, TP44, TP45, TP46, TP47, TP48, TP49, TP5, TP50, TP51, TP52, TP53, TP54, TP55, TP56, TP57, TP58, TP59, TP6, TP60, TP61, TP62, TP63, TP64, TP65, TP66, TP67, TP68, TP69, TP7, TP70, TP71, TP72, TP73, TP74, TP75, TP76, TP77, TP78, TP79, TP8, TP80, TP81, TP82, TP83, TP84, TP85, TP86, TP87, TP88, TP89, TP9, TP90, TP91, TP92, TP93, TP94, TP95, TP96, TP97, TP98, TP99: TestPoint, SWS-Library:SWS-Testpoint-Bug-1mm, symbol Connector:TestPoint
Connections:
- net LEDS_CANADA_LINE_NORTH_TO_SOUTH: now also TP110.1
- net LEDS_CANADA_LINE_SOUTH_TO_NORTH: now also TP94.1
- net LEDS_EXPO_LINE_WEST_TO_EAST: now also TP24.1
- net LEDS_MILLENNIUM_LINE_EAST_TO_WEST: now also TP48.1
- net LEDS_MILLENNIUM_LINE_WEST_TO_EAST: now also TP71.1
- net LEDS_SEA_BUS: now also TP126.1
- net at LED80.1 (DOUT), LED81.4 (DIN): now also TP80.1
- net at LED79.1 (DOUT), LED80.4 (DIN): now also TP79.1
- net at LED69.1 (DOUT), LED70.4 (DIN): now also TP69.1
- net at LED68.1 (DOUT), LED69.4 (DIN): now also TP68.1
- net at LED23.1 (DOUT), LED24.4 (DIN): now also TP23.1
- net at LED22.1 (DOUT), LED23.4 (DIN): now also TP22.1
- net at LED19.1 (DOUT), LED20.4 (DIN): now also TP19.1
- net at LED18.1 (DOUT), LED19.4 (DIN): now also TP18.1
- net at LED27.1 (DOUT), LED28.4 (DIN): now also TP27.1
- net at LED26.1 (DOUT), LED27.4 (DIN): now also TP26.1
- net at LED77.1 (DOUT), LED78.4 (DIN): now also TP77.1
- net at LED76.1 (DOUT), LED77.4 (DIN): now also TP76.1
- net at LED90.1 (DOUT), LED91.4 (DIN): now also TP90.1
- net at LED89.1 (DOUT), LED90.4 (DIN): now also TP89.1
- net at LED42.1 (DOUT), LED43.4 (DIN): now also TP42.1
- net at LED41.1 (DOUT), LED42.4 (DIN): now also TP41.1
- net at LED73.1 (DOUT), LED74.4 (DIN): now also TP73.1
- net at LED72.1 (DOUT), LED73.4 (DIN): now also TP72.1
- net at LED124.1 (DOUT), LED125.4 (DIN): now also TP124.1
- net at LED123.1 (DOUT), LED124.4 (DIN): now also TP123.1
- net at LED17.1 (DOUT), LED18.4 (DIN): now also TP17.1
- net at LED109.1 (DOUT), LED110.4 (DIN): now also TP109.1
- net at LED108.1 (DOUT), LED109.4 (DIN): now also TP108.1
- net at LED29.1 (DOUT), LED30.4 (DIN): now also TP29.1
- net at LED28.1 (DOUT), LED29.4 (DIN): now also TP28.1
- net at LED53.1 (DOUT), LED54.4 (DIN): now also TP53.1
- net at LED52.1 (DOUT), LED53.4 (DIN): now also TP52.1
- net at LED16.1 (DOUT), LED17.4 (DIN): now also TP16.1
- net at LED112.1 (DOUT), LED113.4 (DIN): now also TP112.1
- net at LED111.1 (DOUT), LED112.4 (DIN): now also TP111.1
- net at LED105.1 (DOUT), LED106.4 (DIN): now also TP105.1
- net at LED104.1 (DOUT), LED105.4 (DIN): now also TP104.1
- net at LED34.1 (DOUT), LED35.4 (DIN): now also TP34.1
- net at LED33.1 (DOUT), LED34.4 (DIN): now also TP33.1
- net at LED40.1 (DOUT), LED41.4 (DIN): now also TP40.1
- net at LED39.1 (DOUT), LED40.4 (DIN): now also TP39.1
- net at LED25.1 (DOUT), LED26.4 (DIN): now also TP25.1
- net at LED120.1 (DOUT), LED121.4 (DIN): now also TP120.1
- net at LED119.1 (DOUT), LED120.4 (DIN): now also TP119.1
- net at LED15.1 (DOUT), LED16.4 (DIN): now also TP15.1
- net at LED14.1 (DOUT), LED15.4 (DIN): now also TP14.1
- net at LED37.1 (DOUT), LED38.4 (DIN): now also TP37.1
- net at LED36.1 (DOUT), LED37.4 (DIN): now also TP36.1
- net at LED10.1 (DOUT), LED11.4 (DIN): now also TP10.1
- net at LED10.4 (DIN), LED9.1 (DOUT): now also TP9.1
- net at LED70.1 (DOUT), LED71.4 (DIN): now also TP70.1
- net at LED8.1 (DOUT), LED9.4 (DIN): now also TP8.1
- net at LED7.1 (DOUT), LED8.4 (DIN): now also TP7.1
- net at LED62.1 (DOUT), LED63.4 (DIN): now also TP62.1
- net at LED61.1 (DOUT), LED62.4 (DIN): now also TP61.1
- net at LED35.1 (DOUT), LED36.4 (DIN): now also TP35.1
- net at LED83.1 (DOUT), LED84.4 (DIN): now also TP83.1
- net at LED82.1 (DOUT), LED83.4 (DIN): now also TP82.1
- net at LED91.1 (DOUT), LED92.4 (DIN): now also TP91.1
- net at LED38.1 (DOUT), LED39.4 (DIN): now also TP38.1
- net at LED87.1 (DOUT), LED88.4 (DIN): now also TP87.1
- net at LED86.1 (DOUT), LED87.4 (DIN): now also TP86.1
- net at LED107.1 (DOUT), LED108.4 (DIN): now also TP107.1
- net at LED49.1 (DOUT), LED50.4 (DIN): now also TP49.1
- net at LED64.1 (DOUT), LED65.4 (DIN): now also TP64.1
- net at LED63.1 (DOUT), LED64.4 (DIN): now also TP63.1
- net at LED45.1 (DOUT), LED46.4 (DIN): now also TP45.1
- net at LED44.1 (DOUT), LED45.4 (DIN): now also TP44.1
- net at LED97.1 (DOUT), LED98.4 (DIN): now also TP97.1
- net at LED96.1 (DOUT), LED97.4 (DIN): now also TP96.1
- net at LED51.1 (DOUT), LED52.4 (DIN): now also TP51.1
- net at LED13.1 (DOUT), LED14.4 (DIN): now also TP13.1
- net at LED125.1 (DOUT), LED126.4 (DIN): now also TP125.1
- net at LED60.1 (DOUT), LED61.4 (DIN): now also TP60.1
- net at LED47.1 (DOUT), LED48.4 (DIN): now also TP47.1
- net at LED95.1 (DOUT), LED96.4 (DIN): now also TP95.1
- net at LED106.1 (DOUT), LED107.4 (DIN): now also TP106.1
- net at LED114.1 (DOUT), LED115.4 (DIN): now also TP114.1
- net at LED113.1 (DOUT), LED114.4 (DIN): now also TP113.1
- net at LED50.1 (DOUT), LED51.4 (DIN): now also TP50.1
- net at LED93.1 (DOUT), LED94.4 (DIN): now also TP93.1
- net at LED92.1 (DOUT), LED93.4 (DIN): now also TP92.1
- net at LED54.1 (DOUT), LED55.4 (DIN): now also TP54.1
- net at LED74.1 (DOUT), LED75.4 (DIN): now also TP74.1
- net at LED4.1 (DOUT), LED5.4 (DIN): now also TP4.1
- net at LED3.1 (DOUT), LED4.4 (DIN): now also TP3.1
- net at LED103.1 (DOUT), LED104.4 (DIN): now also TP103.1
- net at LED102.1 (DOUT), LED103.4 (DIN): now also TP102.1
- net at LED117.1 (DOUT), LED118.4 (DIN): now also TP117.1
- net at LED116.1 (DOUT), LED117.4 (DIN): now also TP116.1
- net at LED46.1 (DOUT), LED47.4 (DIN): now also TP46.1
- net at LED12.1 (DOUT), LED13.4 (DIN): now also TP12.1
- net at LED11.1 (DOUT), LED12.4 (DIN): now also TP11.1
- net at LED75.1 (DOUT), LED76.4 (DIN): now also TP75.1
- net at LED121.1 (DOUT), LED122.4 (DIN): now also TP121.1
- net at LED56.1 (DOUT), LED57.4 (DIN): now also TP56.1
- net at LED55.1 (DOUT), LED56.4 (DIN): now also TP55.1
- net at LED81.1 (DOUT), LED82.4 (DIN): now also TP81.1
- net at LED43.1 (DOUT), LED44.4 (DIN): now also TP43.1
- net at LED118.1 (DOUT), LED119.4 (DIN): now also TP118.1
- net at LED85.1 (DOUT), LED86.4 (DIN): now also TP85.1
- net at LED66.1 (DOUT), LED67.4 (DIN): now also TP66.1
- net at LED65.1 (DOUT), LED66.4 (DIN): now also TP65.1
- net at LED98.1 (DOUT), LED99.4 (DIN): now also TP98.1
- net at LED100.4 (DIN), LED99.1 (DOUT): now also TP99.1
- net at LED115.1 (DOUT), LED116.4 (DIN): now also TP115.1
- net at LED6.1 (DOUT), LED7.4 (DIN): now also TP6.1
- net at LED5.1 (DOUT), LED6.4 (DIN): now also TP5.1
- net at LED21.1 (DOUT), LED22.4 (DIN): now also TP21.1
- net at LED20.1 (DOUT), LED21.4 (DIN): now also TP20.1
- net at LED32.1 (DOUT), LED33.4 (DIN): now also TP32.1
- net at LED67.1 (DOUT), LED68.4 (DIN): now also TP67.1
- net at LED101.1 (DOUT), LED102.4 (DIN): now also TP101.1
- net at LED1.1 (DOUT), LED2.4 (DIN): now also TP1.1
- net at LED88.1 (DOUT), LED89.4 (DIN): now also TP88.1
- net at LED31.1 (DOUT), LED32.4 (DIN): now also TP31.1
- net at LED30.1 (DOUT), LED31.4 (DIN): now also TP30.1
- net at LED57.1 (DOUT), LED58.4 (DIN): now also TP57.1
- net at LED84.1 (DOUT), LED85.4 (DIN): now also TP84.1
- net at LED58.1 (DOUT), LED59.4 (DIN): now also TP58.1
- net at LED122.1 (DOUT), LED123.4 (DIN): now also TP122.1
- net at LED100.1 (DOUT), LED101.4 (DIN): now also TP100.1
- net at LED78.1 (DOUT), LED79.4 (DIN): now also TP78.1
- net at LED59.1 (DOUT), LED60.4 (DIN): now also TP59.1
- net at LED2.1 (DOUT), LED3.4 (DIN): now also TP2.1
